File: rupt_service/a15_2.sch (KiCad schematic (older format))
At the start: 38 parts, among them U15016 74LVC07, U15022 74HC04, U15027 74HC02, U15028 74HC27, U15029 74HC02, U15030 74HC27, U15031 74HC27, U15032 74HC27, U15033 74HC02, U15034 74HC27, U15035 74HC27, U15036 74HC27, U15037 74HC02, U15038 74HC27, U15039 74LVC07, U15040 74HC27, U15041 74HC4002, U15042 74HC27, U15043 74HC02, U15044 74HC04, U15045 74HC02, U15046 74HC27, U15047 74HC27, U15048 74HC02, U15049 74HC04, U15050 74HC27, U15051 74HC27, U15052 74HC27, U15053 74HC04, U15054 74HC27, U15055 74HC27, U15056 74HC02, U15057 74HC02, U15058 74HC27, U15059 74HC04, U15060 74HC02

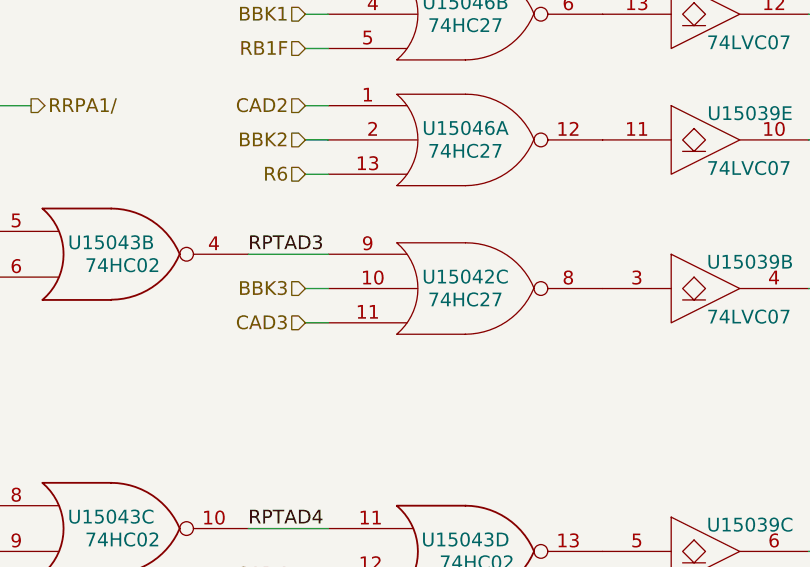
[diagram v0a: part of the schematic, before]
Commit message: Did another pass through the schematics and added in some missing gates
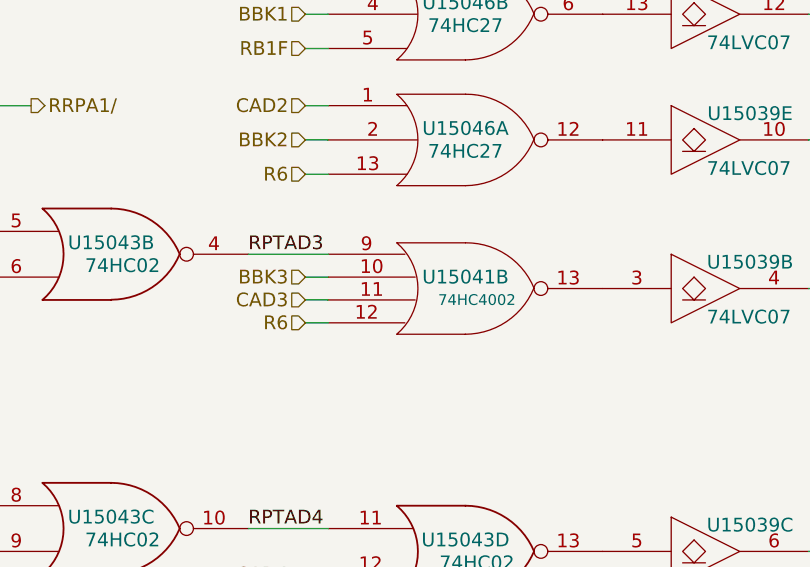
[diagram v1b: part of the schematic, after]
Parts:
- removed unit 3 of U15042
- added unit 2 of U15041
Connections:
- net BBK3: now also U15041.10
- net CAD3: now also U15041.11
- net GND: now also U15041.7 (GND)
- net R6: now also U15041.12
- net RPTAD3: now also U15041.9
- net VCC: now also U15041.14 (VCC)
- net at U15039.3: now also U15041.13
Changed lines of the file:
@@
 Text HLabel 9400 3950 0    60   Input ~ 0
 PRPOR4
-$Comp
-L 74HC27 U15042
-U 3 1 56EB43C9
-P 15000 2200
-F 0 "U15042" H 15000 2250 60  0000 C CNN
-F 1 "74HC27" H 15000 2150 60  0000 C CNN
-F 2 "" H 15000 2200 60  0000 C CNN
-F 3 "" H 15000 2200 60  0000 C CNN
-	3    15000 2200
-	1    0    0    -1
-$EndComp
-Text HLabel 14300 2200 0    60   Input ~ 0
+Text HLabel 14300 2150 0    60   Input ~ 0
 BBK3
-Text HLabel 14300 2350 0    60   Input ~ 0
+Text HLabel 14300 2250 0    60   Input ~ 0
 CAD3
 $Comp
@@
 	10200 3950 9400 3950
 Wire Wire Line
-	14400 2200 14300 2200
-Wire Wire Line
-	14400 2350 14300 2350
+	14400 2150 14300 2150
+Wire Wire Line
+	14400 2250 14300 2250
 Wire Wire Line
 	16500 2200 16650 2200
@@
 Wire Wire Line
 	12850 5900 11350 5900
+$Comp
+L 74HC4002 U15041
+U 2 1 5721B244
+P 15000 2200
+F 0 "U15041" H 15000 2250 60  0000 C CNN
+F 1 "74HC4002" H 15050 2150 47  0000 C CNN
+F 2 "" H 15000 2200 60  0000 C CNN
+F 3 "" H 15000 2200 60  0000 C CNN
+	2    15000 2200
+	1    0    0    -1
+$EndComp
+Text HLabel 14300 2350 0    60   Input ~ 0
+R6
+Wire Wire Line
+	14400 2350 14300 2350
 $EndSCHEMATC

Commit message: Fixed not->1-input nor in the rest of the modules.
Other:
- moved on the sheet: R15001, R15002, U15016D, U15016E, U15016F, U15022B, U15022C, U15022D, U15022E, U15022F, U15027D, U15028A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

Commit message: Updated Rupt Service to be on +4VSW
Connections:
- net labels added: +4VSW
- net labels removed: VCC

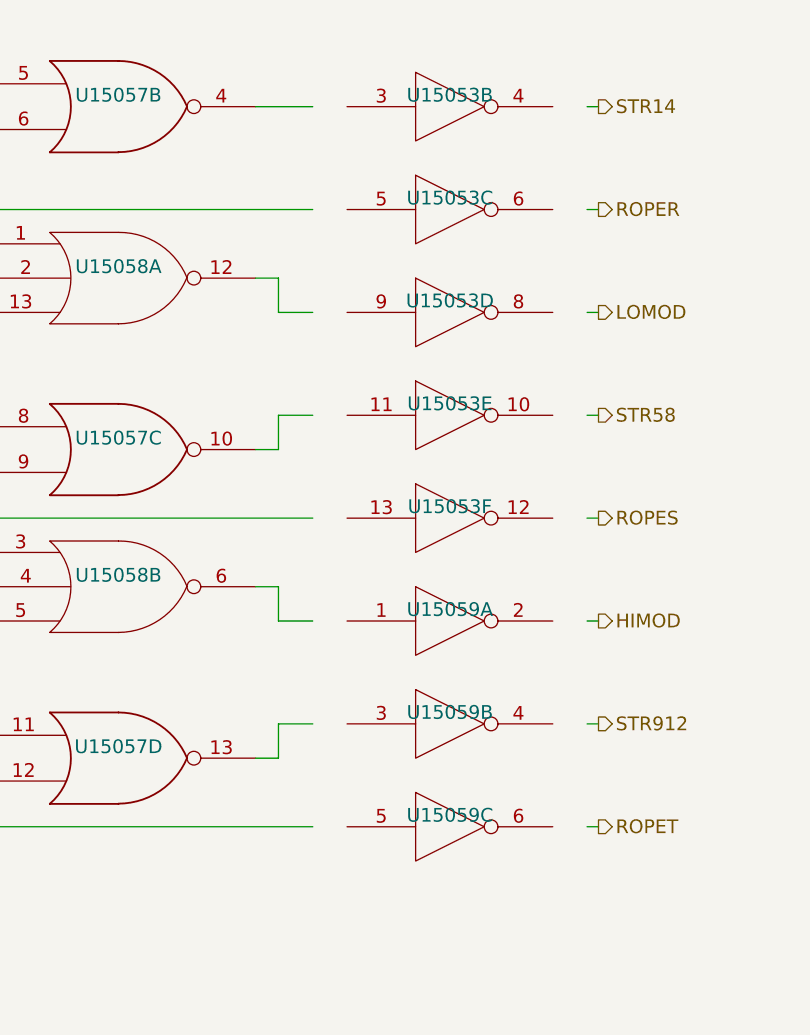
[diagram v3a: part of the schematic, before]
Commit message: This adds fixes to the schematics for changes identified in comparing against the independent AGC schematics in the "schematics" branch of the main Virtual AGC repository.  Changes include:  Topological (but not logical) fixes to the DKCTR4,5,4/,5/ signals in the inout_v schematic. Wiring fix (incorrect signal sources for 5 gates) in inout_iv. Fixed incorrect signal source (including MGOJAM output polarity) for one gate in timer.  Fixed incorrect topology (but not logic) for 3 output signals in service_gates. Fixed backplane signal source (MYCLMP incorrectly used everywhere in place of the correct STRT2) in memory_timing_addressing.  ROPER, ROPES, ROPET had incorrectly omitted STRT2 as an input signal in four_bit_2. A couple of  internal nets local to sheets were also renamed due to conflicts with analysis software.  None of these fixes had any measurable effect on instruction execution; Validation was passed prior to the fixes, and continues to be passed after the fixes, and the identical instruction sequence occurs in doing so.
For me, warnings about missing components from the libraries occur upon every schematic load, though
these missing components don't seem to actually be in the circuits.  I tried to make some library
changes to work around that.  My changes don't actually fix the problem, but rather than try to back
them out and redo all the testing, they're a part of this commit as well.
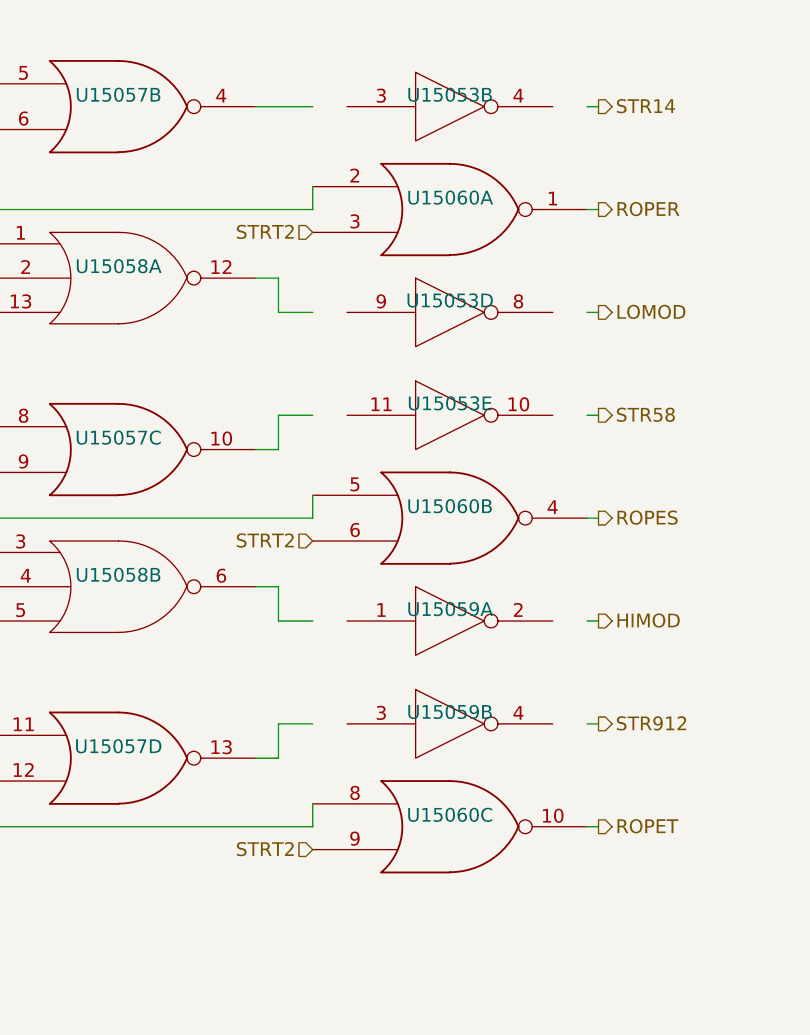
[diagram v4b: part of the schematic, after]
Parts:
- removed unit 3 of U15053
- removed unit 6 of U15053
- removed unit 3 of U15059
- added unit 1 of U15060
- added unit 3 of U15060
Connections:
- net labels added: STRT2
- wire segments 421 -> 424
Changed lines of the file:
@@
 LIBS:valves
 LIBS:rupt_service-cache
-EELAYER 25 0
+EELAYER 26 0
 EELAYER END
 $Descr A1 33110 23386
@@
 	1    0    0    -1
 $EndComp
-$Comp
-L 74HC04 U15053
-U 3 1 56F8C5CA
-P 27900 9900
-AR Path="/56F8C5CA" Ref="U15053"  Part="3"
-AR Path="/56E5D485/56F8C5CA" Ref="U15053"  Part="3"
-F 0 "U15053" H 27900 9950 60  0000 C CNN
-F 1 "74HC04" H 27900 9650 60  0001 C CNN
-F 2 "" H 27900 9900 60  0000 C CNN
-F 3 "" H 27900 9900 60  0000 C CNN
-	3    27900 9900
-	1    0    0    -1
-$EndComp
 Wire Wire Line
 	28500 9450 28550 9450
@@
 Wire Wire Line
 	27150 10800 27300 10800
-$Comp
-L 74HC04 U15053
-U 6 1 56F94794
-P 27900 11250
-AR Path="/56F94794" Ref="U15053"  Part="6"
-AR Path="/56E5D485/56F94794" Ref="U15053"  Part="6"
-F 0 "U15053" H 27900 11300 60  0000 C CNN
-F 1 "74HC04" H 27900 11000 60  0001 C CNN
-F 2 "" H 27900 11250 60  0000 C CNN
-F 3 "" H 27900 11250 60  0000 C CNN
-	6    27900 11250
-	1    0    0    -1
-$EndComp
 Wire Wire Line
 	28500 11250 28550 11250
@@
 Wire Wire Line
 	27150 12300 27050 12300
-$Comp
-L 74HC04 U15059
-U 3 1 56F9754F
-P 27900 12600
-AR Path="/56F9754F" Ref="U15059"  Part="3"
-AR Path="/56E5D485/56F9754F" Ref="U15059"  Part="3"
-F 0 "U15059" H 27900 12650 60  0000 C CNN
-F 1 "74HC04" H 27900 12350 60  0001 C CNN
-F 2 "" H 27900 12600 60  0000 C CNN
-F 3 "" H 27900 12600 60  0000 C CNN
-	3    27900 12600
-	1    0    0    -1
-$EndComp
 Wire Wire Line
 	28500 12600 28550 12600
@@
 	1    0    0    -1
 $EndComp
+$Comp
+L 74HC02 U?
+U 1 1 5BD8C0D7
+P 27900 9900
+AR Path="/5BD8C0D7" Ref="U?"  Part="2"
+AR Path="/56E5D485/5BD8C0D7" Ref="U15060"  Part="1"
+F 0 "U15060" H 27900 9950 60  0000 C CNN
+F 1 "74HC02" H 27950 9850 60  0001 C CNN
+F 2 "" H 27900 9900 60  0000 C CNN
+F 3 "" H 27900 9900 60  0000 C CNN
+	1    27900 9900
+	1    0    0    -1
+$EndComp
+Wire Wire Line
+	27300 9900 27300 9800
+Text HLabel 27300 10000 0    60   Input ~ 0
+STRT2
+$Comp
+L 74HC02 U?
+U 2 1 5BD8C753
+P 27900 11250
+AR Path="/5BD8C753" Ref="U?"  Part="2"
+AR Path="/56E5D485/5BD8C753" Ref="U15060"  Part="2"
+F 0 "U15060" H 27900 11300 60  0000 C CNN
+F 1 "74HC02" H 27950 11200 60  0001 C CNN
+F 2 "" H 27900 11250 60  0000 C CNN
+F 3 "" H 27900 11250 60  0000 C CNN
+	2    27900 11250
+	1    0    0    -1
+$EndComp
+$Comp
+L 74HC02 U?
+U 3 1 5BD8C8C5
+P 27900 12600
+AR Path="/5BD8C8C5" Ref="U?"  Part="2"
+AR Path="/56E5D485/5BD8C8C5" Ref="U15060"  Part="3"
+F 0 "U15060" H 27900 12650 60  0000 C CNN
+F 1 "74HC02" H 27950 12550 60  0001 C CNN
+F 2 "" H 27900 12600 60  0000 C CNN
+F 3 "" H 27900 12600 60  0000 C CNN
+	3    27900 12600
+	1    0    0    -1
+$EndComp
+Wire Wire Line
+	27300 11250 27300 11150
+Wire Wire Line
+	27300 12600 27300 12500
+Text HLabel 27300 11350 0    60   Input ~ 0
+STRT2
+Text HLabel 27300 12700 0    60   Input ~ 0
+STRT2
 $EndSCHEMATC
